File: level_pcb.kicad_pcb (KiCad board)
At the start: 2 copper layers, 100 x 100 mm, 76 parts, among them J1 Output-Thru, J2 AudioJack3, J3 Conn_01x20, J4 Conn_01x20, J5 Conn_02x05_Odd_Even, J6 Conn_01x20, U1 ARDUINO_PRO_MINI_custom, U2 LM7805_TO220

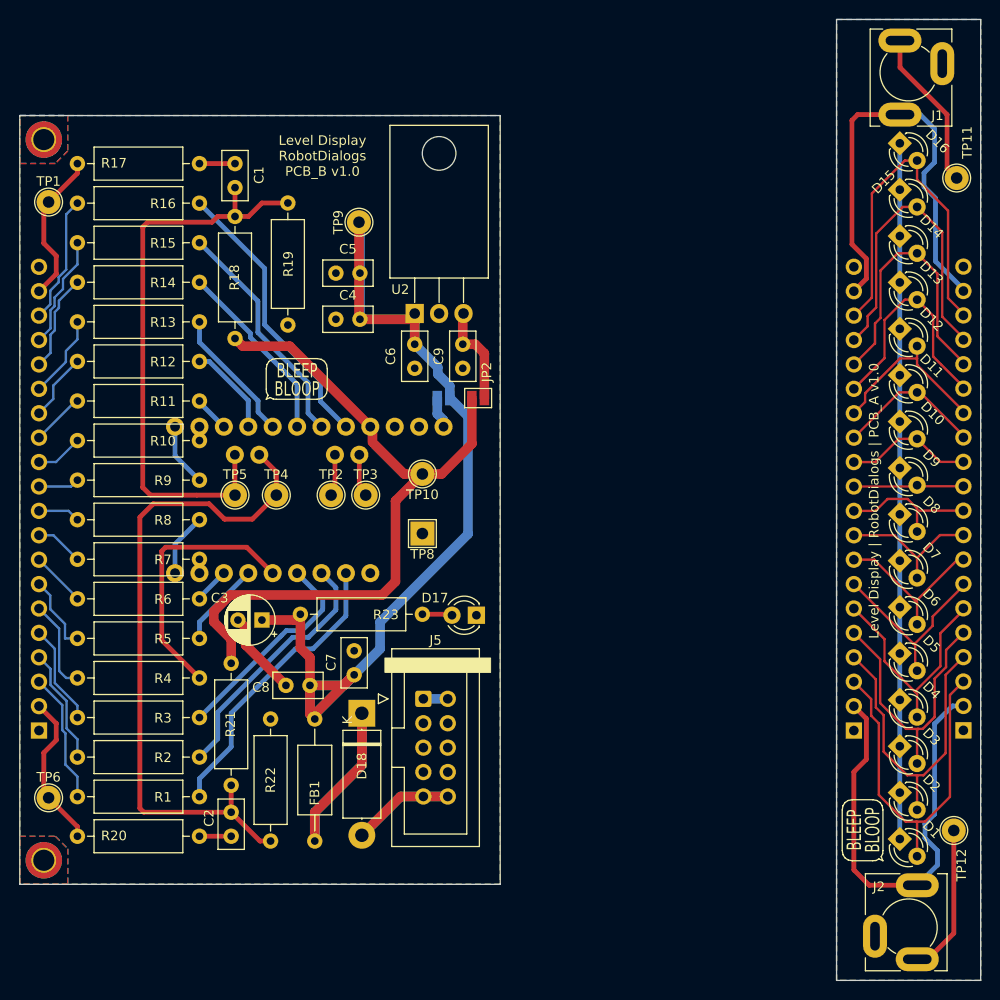
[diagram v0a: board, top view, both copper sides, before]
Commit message: Version 2 PCB as ordered
Switch to KiCAD v6
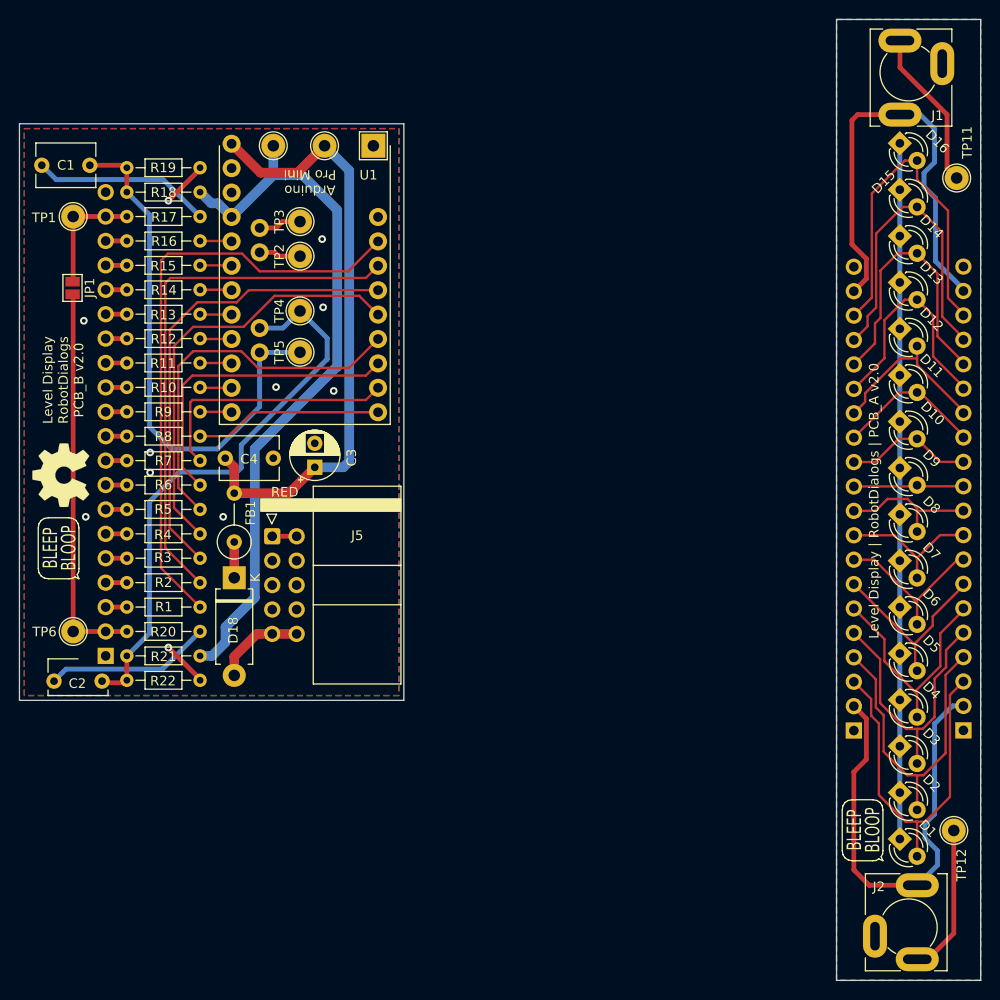
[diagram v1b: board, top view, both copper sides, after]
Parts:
- removed C5, C6, C7, C8, C9: 100nF, Capacitor_THT:C_Disc_D5.0mm_W2.5mm_P2.50mm
- removed D17: LED 1, My Stuff:LED_D3.0mm
- removed H1, H2: MountingHole_Pad, MountingHole:MountingHole_2.2mm_M2_DIN965_Pad_TopBottom
- removed JP2: Jumper_NO_Small, Jumper:SolderJumper-2_P1.3mm_Open_Pad1.0x1.5mm
- removed R23: 1k, My Stuff:R_Axial_DIN0309_L9.0mm_D3.2mm_P12.70mm_Horizontal
- removed U2: LM7805_TO220, Package_TO_SOT_THT:TO-220-3_Horizontal_TabDown
- added LOGO2: logo1, My Stuff:Logo1, F.Cu at (226.2, 127.9)
- added LOGO2: logo1, My Stuff:Logo1, B.Cu at (226.2, 127.9)
- added LOGO3: Logo_Open_Hardware_Small, Symbol:OSHW-Symbol_6.7x6mm_SilkScreen, F.Cu at (142.8, 90.9)
- added LOGO3: Logo_Open_Hardware_Small, Symbol:OSHW-Symbol_6.7x6mm_SilkScreen, B.Cu at (142.8, 84.4)
- added X1: Level_Display_Front_Panel, My Stuff:Level_Display_Front_Panel, F.Cu at (223.5, 143.5)
- C1, C2, C4: footprint Capacitor_THT:C_Disc_D5.0mm_W2.5mm_P2.50mm -> Capacitor_THT:C_Disc_D6.0mm_W4.4mm_P5.00mm
- D18: footprint Diode_THT:D_5W_P12.70mm_Horizontal -> Diode_THT:D_DO-15_P10.16mm_Horizontal
- FB1: footprint Inductor_THT:L_Axial_L7.0mm_D3.3mm_P12.70mm_Horizontal_Fastron_MICC -> Inductor_THT:L_Axial_L7.0mm_D3.3mm_P5.08mm_Vertical_Fastron_MICC
- J5: footprint Connector_IDC:IDC-Header_2x05_P2.54mm_Vertical -> Connector_IDC:IDC-Header_2x05_P2.54mm_Horizontal
- JP1: value Jumper_NO_Small -> SolderJumper_2_Open; moved to F.Cu
- LOGO1: moved to B.Cu
- R1, R10, R11, R12, R13, R14, R15, R16, R17, R18, R19, R2, R20, R21, R22, R3, R4, R5, R6, R7, R8, R9: footprint My Stuff:R_Axial_DIN0309_L9.0mm_D3.2mm_P12.70mm_Horizontal -> Resistor_THT:R_Axial_DIN0204_L3.6mm_D1.6mm_P7.62mm_Horizontal
- moved LOGO1 54.3 mm to (175.2, 109.5)
- moved TP8 40.7 mm to (175.3, 56.6), turned to -90 degrees
- moved JP1 40.3 mm to (144.0, 71.4), turned to -90 degrees
- moved TP10 37.5 mm to (164.9, 56.6), turned to -90 degrees
- moved FB1 32.2 mm to (160.8, 97.9)
- moved LOGO1 30.4 mm to (142.5, 98.6), turned to 90 degrees
- moved TP3 29.3 mm to (167.7, 64.5), turned to 90 degrees
- moved TP2 25.1 mm to (167.7, 68.1), turned to 90 degrees
- moved U1 24.4 mm to (168.2, 69.1), turned to 180 degrees
- moved J5 23.1 mm to (164.8, 97.3)
- moved R20 21.3 mm to (157.3, 107.2)
- moved R1 20.4 mm to (149.6, 104.7)
- moved D18 19.4 mm to (160.8, 101.6)
- moved TP4 19.3 mm to (167.7, 73.8), turned to 90 degrees
- moved C2 19.1 mm to (147.1, 112.4), turned to 180 degrees
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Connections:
- JP1 pad 1: +12V -> Net-(J4-Pad19)
- JP1 pad 2: Net-(JP1-Pad2) -> Net-(J4-Pad2)
- U1 pad JP6_1: Net-(JP1-Pad2) -> +12V
- U1 pad JP6_3: Net-(U1-PadJP6_3) -> unconnected-(U1-PadJP6_3)
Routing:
- net +12V: track 122.5 -> 63.4 mm
- net Net-(R1-Pad2): track 30.6 -> 62.7 mm
- net Net-(R5-Pad2): track 8.90 -> 39.2 mm
- net Net-(R2-Pad2): track 26.6 -> 55.6 mm
- net Net-(R6-Pad2): track 3.73 -> 32.4 mm
- net Net-(D18-Pad1): track 30.7 -> 3.72 mm
- net Net-(R16-Pad2): track 29.6 -> 3.30 mm
- net Net-(R3-Pad2): track 22.4 -> 48.5 mm
- net Net-(R7-Pad2): track 1.44 -> 26.7 mm
- net Net-(J4-Pad2): track 16.3 -> 40.5 mm
- net Net-(R15-Pad2): track 24.4 -> 3.30 mm
- net Net-(R4-Pad2): track 27.7 -> 44.9 mm
- net Net-(R14-Pad2): track 19.2 -> 3.30 mm
- net Net-(C1-Pad2): track 3.70 -> 18.7 mm
- net Net-(C2-Pad2): track 3.30 -> 17.4 mm
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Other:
- outline, holes or cut-outs redrawn
- net class Default removed
- board text added: "Level Display RobotDialogs PCB_B v2.0"
- board text added: "Level Display | RobotDialogs | PCB_A v2.0"
- board text removed: "Level Display RobotDialogs PCB_B v1.0"
- board text removed: "Level Display | RobotDialogs | PCB_A v1.0"
